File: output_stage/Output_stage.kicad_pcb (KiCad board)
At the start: 2 copper layers, 62.9 x 27.9 mm, 16 parts, among them J1 Conn_01x03_Socket, J2 Control/LED, J3 Control/LED, Q1 BTA41, U1 MOC3043M

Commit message: Add 3D copper strap models to output stage board
Two 1.5mm² copper straps (LINE and S/LINE) connecting J1 Phoenix
connector to Q1 triac via REF test pads. Straps traverse the PCB
twice through drill holes. Generated with cadquery (generate_straps.py).
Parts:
- added G_LINE: CopperStrap_LINE, UserDef:CopperStrap_LINE, F.Cu at (82.3, 39.4)
- added G_SLINE: CopperStrap_SLINE, UserDef:CopperStrap_SLINE, F.Cu at (82.3, 39.4)
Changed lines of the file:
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@@
 		(embedded_fonts no)
+	)
+	(footprint "UserDef:CopperStrap_LINE"
+		(layer "F.Cu")
+		(at 82.285225 39.368075)
+		(descr "1.5mm² copper strap for LINE net")
+		(property "Reference" "G_LINE"
+			(at 0 0 0)
+			(layer "F.SilkS")
+			(hide yes)
+			(effects
+				(font
+					(size 1 1)
+					(thickness 0.15)
+				)
+			)
+		)
+		(property "Value" "CopperStrap_LINE"
+			(at 0 0 0)
+			(layer "F.Fab")
+			(hide yes)
+			(effects
+				(font
+					(size 1 1)
+					(thickness 0.15)
+				)
+			)
+		)
+		(property "Datasheet" ""
+			(at 0 0 0)
+			(layer "F.Fab")
+			(hide yes)
+			(effects
+				(font
+					(size 1.27 1.27)
+					(thickness 0.15)
+				)
+			)
+		)
+		(property "Description" ""
+			(at 0 0 0)
+			(layer "F.Fab")
+			(hide yes)
+			(effects
+				(font
+					(size 1.27 1.27)
+					(thickness 0.15)
+				)
+			)
+		)
+		(attr board_only exclude_from_pos_files exclude_from_bom allow_missing_courtyard)
+		(embedded_fonts no)
+		(model "${KIPRJMOD}/../KiCad/3dmodels/CopperStrap_LINE.step"
+			(offset
+				(xyz 0 0 -1.75)
+			)
+			(scale
+				(xyz 1 1 1)
+			)
+			(rotate
+				(xyz -0 -0 -0)
+			)
+		)
+	)
+	(footprint "UserDef:CopperStrap_SLINE"
+		(layer "F.Cu")
+		(at 82.285225 39.368075)
+		(descr "1.5mm² copper strap for S/LINE net")
+		(property "Reference" "G_SLINE"
+			(at 0 0 0)
+			(layer "F.SilkS")
+			(hide yes)
+			(effects
+				(font
+					(size 1 1)
+					(thickness 0.15)
+				)
+			)
+		)
+		(property "Value" "CopperStrap_SLINE"
+			(at 0 0 0)
+			(layer "F.Fab")
+			(hide yes)
+			(effects
+				(font
+					(size 1 1)
+					(thickness 0.15)
+				)
+			)
+		)
+		(property "Datasheet" ""
+			(at 0 0 0)
+			(layer "F.Fab")
+			(hide yes)
+			(effects
+				(font
+					(size 1.27 1.27)
+					(thickness 0.15)
+				)
+			)
+		)
+		(property "Description" ""
+			(at 0 0 0)
+			(layer "F.Fab")
+			(hide yes)
+			(effects
+				(font
+					(size 1.27 1.27)
+					(thickness 0.15)
+				)
+			)
+		)
+		(attr board_only exclude_from_pos_files exclude_from_bom allow_missing_courtyard)
+		(embedded_fonts no)
+		(model "${KIPRJMOD}/../KiCad/3dmodels/CopperStrap_SLINE.step"
+			(offset
+				(xyz 0 0 -1.75)
+			)
+			(scale
+				(xyz 1 1 1)
+			)
+			(rotate
+				(xyz -0 -0 -0)
+			)
+		)
 	)
 	(footprint "Connector_Phoenix_MSTB:PhoenixContact_MSTBVA_2,5_3-G-5,08_1x03_P5.08mm_Vertical"
@@
 	)
 	(group ""
-		(members "16cb0a7b-5fea-4076-9bf0-48e4004753c5" "239a6d10-6794-4df0-9b10-e9041655458f"
-			"679e3237-7688-4bcf-a1c1-bff8bb1d3c0d" "9844d608-e51d-433b-9200-d108d913eb21"
-			"9b2e0c26-f93d-4a48-84a1-e7b2d725e332" "a9d12b21-bc01-4bee-9d36-d2c9e5442e5c"
-			"d599bc64-a24e-403e-80ce-3a6d5d16232e" "de8476e6-dbd2-4ca2-bf91-2888436c8027"
-			"f8ddf2a0-7f7d-4757-8d02-9c6ef70becfd" "fb7f242f-958a-40f2-a35e-943180f70576"
-		)
+		(members "16cb0a7b-5fea-4076-9bf0-48e4004753c5" "a9d12b21-bc01-4bee-9d36-d2c9e5442e5c")
 	)
 	(group ""
@@
 	(group ""
 		(members "1051a3e7-3320-4661-b3eb-1f5c36a13d8b" "18593530-90a6-4c5b-bc3a-22d7379a7b24"
-			"43a89f31-4873-404a-b8fc-53c722f6611b" "48b8c307-c78f-404f-a4d8-e78ce59abcfc"
 			"4f3e17a5-5a49-483c-951e-6b19ce4081b5" "8d84c98c-b127-4445-93f5-586064a21888"
-			"91f61ad2-d6a0-4338-a740-29825e5ac796" "dc3c2453-e9df-4be7-9941-91bf9437bc34"
-			"e24caffc-d03c-4889-9e74-07f064892c14" "eb910776-dd11-4ae9-8775-948cde81ffb6"
-		)
-	)
+		)
+	)

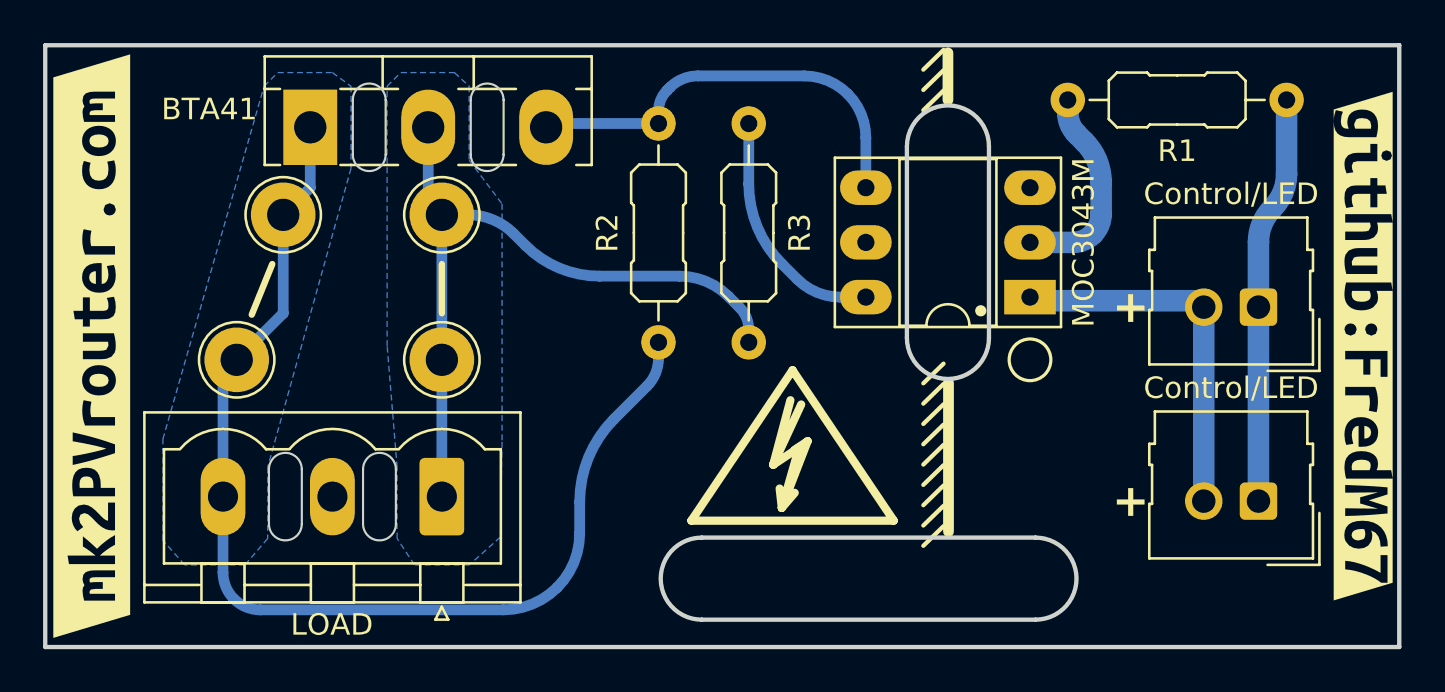
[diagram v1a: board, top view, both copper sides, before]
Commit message: Rework copper strap footprints with real THT pads
Replace 4 standalone REF test pads with 2 proper CopperStrap footprints
(W1/W2) having real THT pads (3mm, 1.5mm drill) on LINE/S_LINE nets.
Footprints include Fab layer artwork showing strap path and 3D STEP
models. Add UserDef library to output_stage fp-lib-table.
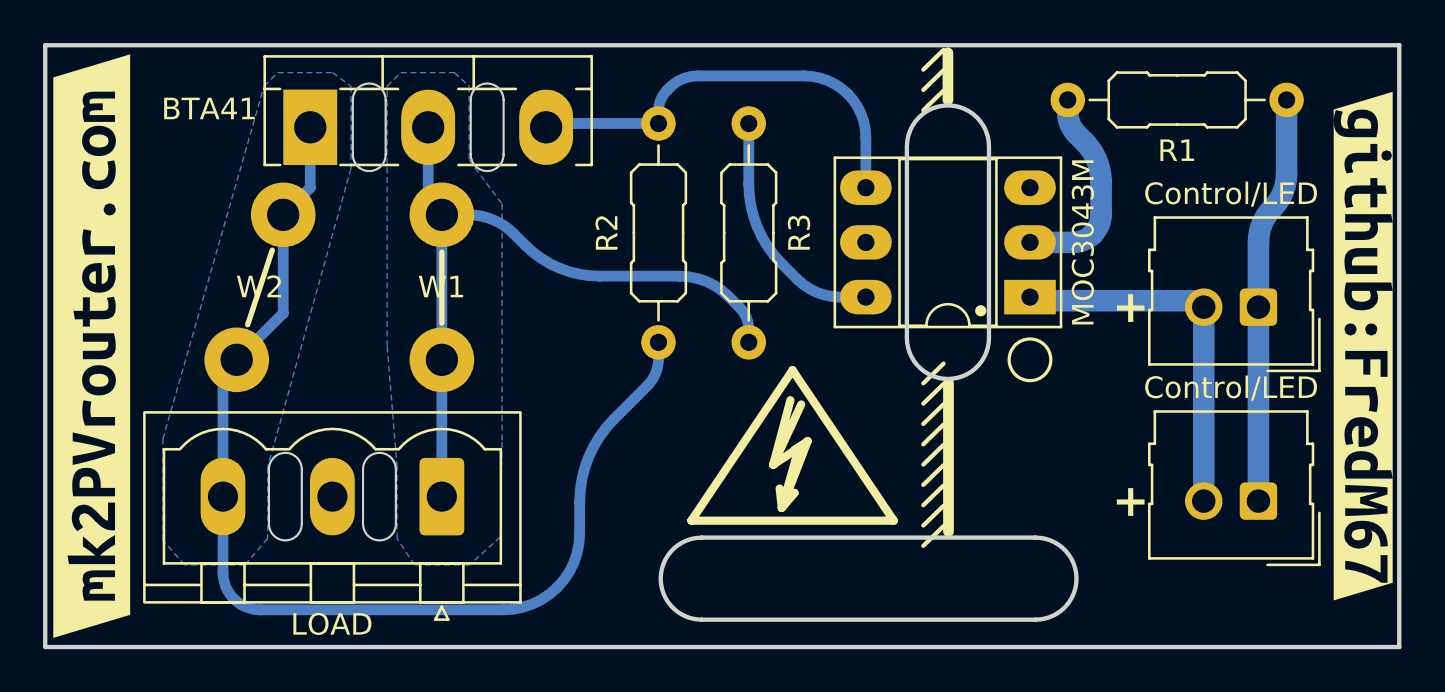
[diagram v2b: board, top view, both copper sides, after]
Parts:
- removed G_LINE: CopperStrap_LINE, UserDef:CopperStrap_LINE
- removed G_SLINE: CopperStrap_SLINE, UserDef:CopperStrap_SLINE
- removed REF1, REF2, REF3, REF4: TestPoint_THTPad_D3.0mm_Drill1.5mm, TestPoint:TestPoint_THTPad_D3.0mm_Drill1.5mm
- added W1: CopperStrap_LINE, UserDef:CopperStrap_LINE, F.Cu at (69.3, 40.0)
- added W2: CopperStrap_SLINE, UserDef:CopperStrap_SLINE, F.Cu at (59.7, 40.0)
